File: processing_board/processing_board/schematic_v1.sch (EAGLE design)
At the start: 22 parts, among them Q1 BSS138, Q2 BSS138

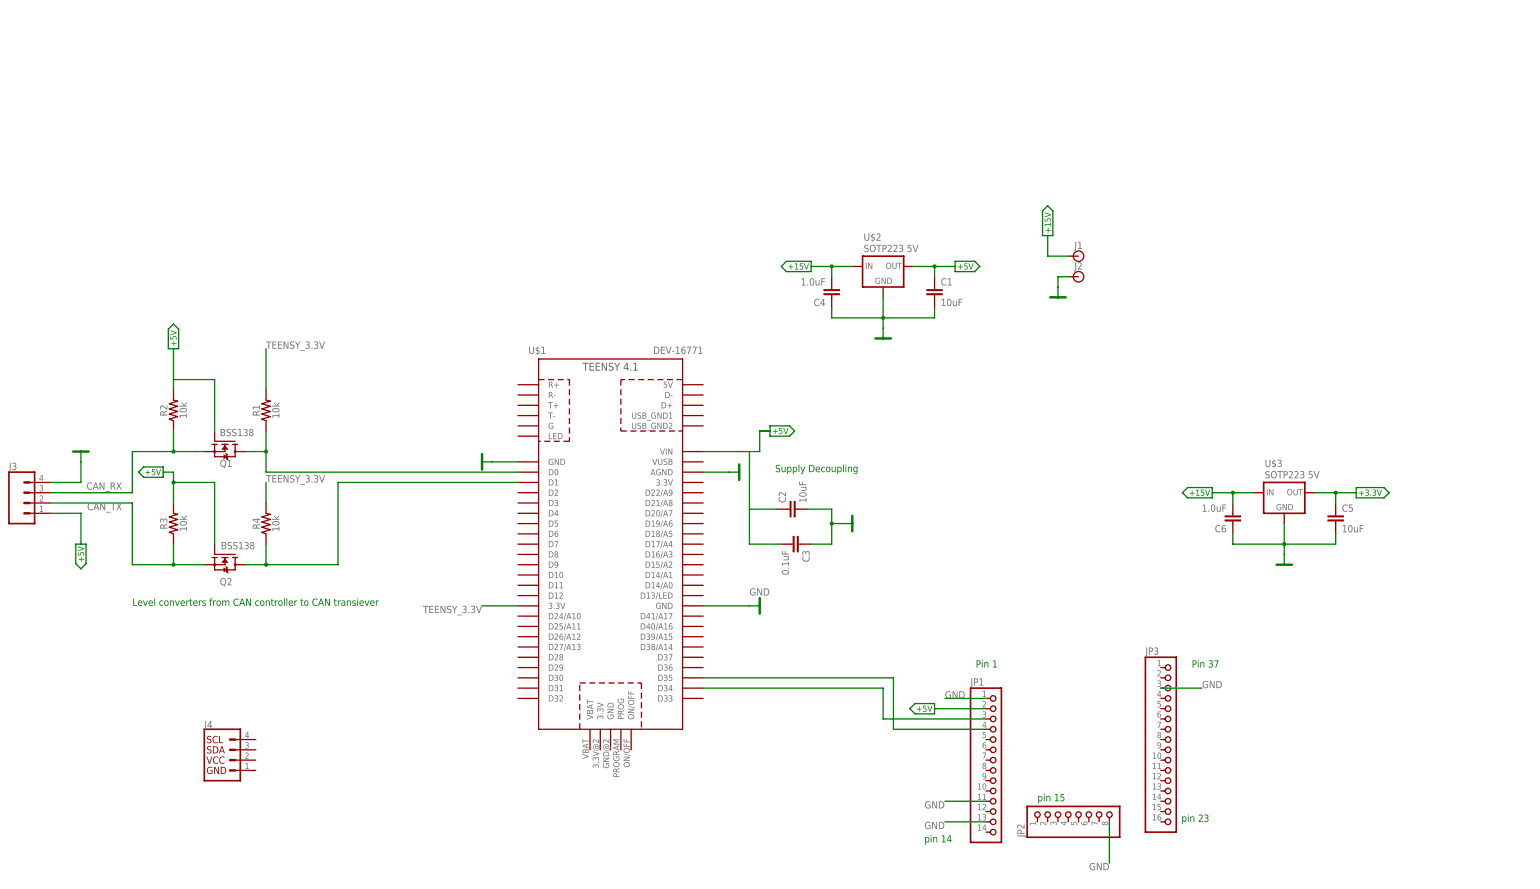
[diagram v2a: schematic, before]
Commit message: added LED
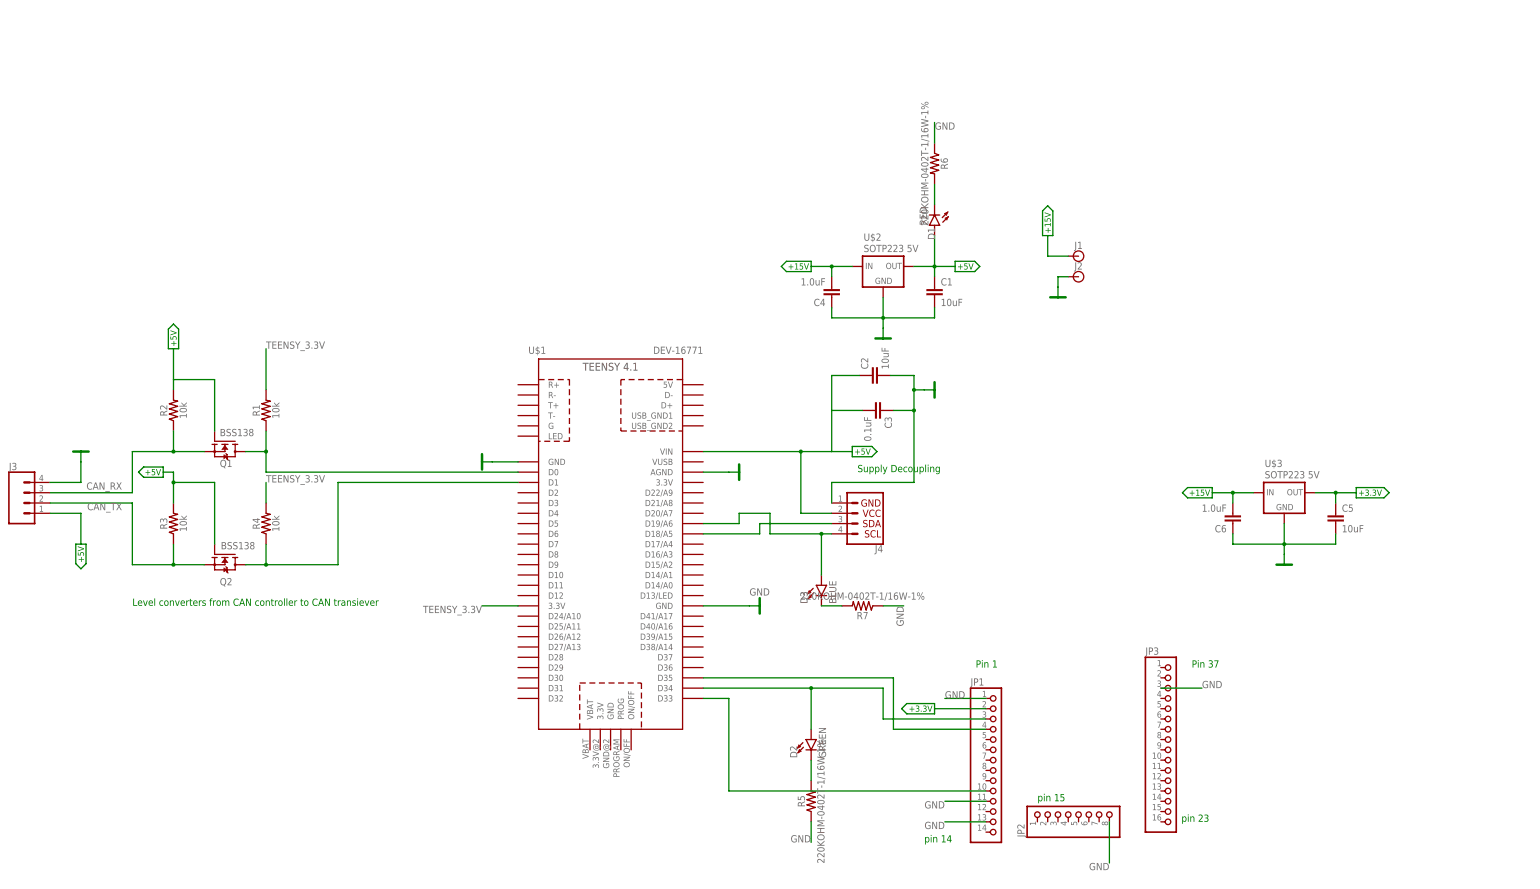
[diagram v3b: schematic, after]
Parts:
- added D1: RED, SparkFun-LED:LED-RED0603
- added D2: GREEN, SparkFun-LED:LED-GREEN0603
- added D3: BLUE, SparkFun-LED:LED-BLUE0603
- added R5, R6, R7: 220KOHM-0402T-1/16W-1%, SparkFun-Resistors:220KOHM-0402T-1/16W-1%
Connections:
- new net N$4: D2.C, R5.2
- new net N$5: J4.3, U$1.D18/A5
- new net N$6: D3.A, J4.4, U$1.D19/A6
- new net N$7: D1.C, R6.2
- new net N$8: D3.C, R7.2
- new net N$9: JP1.10, U$1.D33
- net +3.3V: now also JP1.2
- net +5V: now also D1.A, J4.2; no longer JP1.2
- net GND: now also J4.1, R5.1, R6.1, R7.1
- net N$2: now also D2.A
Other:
- moved on the sheet: C2, C3, J4

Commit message: updated schematic
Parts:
- added D4: RED, SparkFun-LED:LED-RED0603
- added D5: GREEN, SparkFun-LED:LED-GREEN0603
- added Q3, Q4: BSS138, BSS138:BSS138
- added R10, R11, R12, R9: 10k, SparkFun-Resistors:10KOHM-0603-1/10W-1%
- added R13, R8: 10K, SparkFun-Resistors:220KOHM-0402T-1/16W-1%
- R5, R6, R7: value 220KOHM-0402T-1/16W-1% -> 10K
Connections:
- removed net N$4: D2.C, R5.2
- removed net N$5: J4.3, U$1.D18/A5
- removed net N$6: D3.A, J4.4, U$1.D19/A6
- removed net N$8: D3.C, R7.2
- new net +5V1: D4.A
- new net CAN_RX1: D3.C, J4.3, Q3.S, R10.1
- new net CAN_TX1: J4.4, Q4.S, R11.1
- new net N$10: D4.C, R8.2
- new net SCL: Q4.D, R12.1, U$1.D19/A6
- new net SDA: Q3.D, R9.1, U$1.D18/A5
- net +3.3V: now also R13.2, R5.2
- net +5V: now also Q3.G, Q4.G, R10.2, R11.2
- net GND: now also R8.1; no longer R5.1, R7.1
- net N$1: now also D5.C
- net N$2: now also D2.C; no longer D2.A
- net TEENSY_3.3V: now also R12.2, R9.2
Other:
- moved on the sheet: C1, C2, C3, C4, C5, C6, D1, D2, D3, J1, J2, J4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
